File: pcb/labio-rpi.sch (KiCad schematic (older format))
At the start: 7 parts, among them P1 CONN_02X20

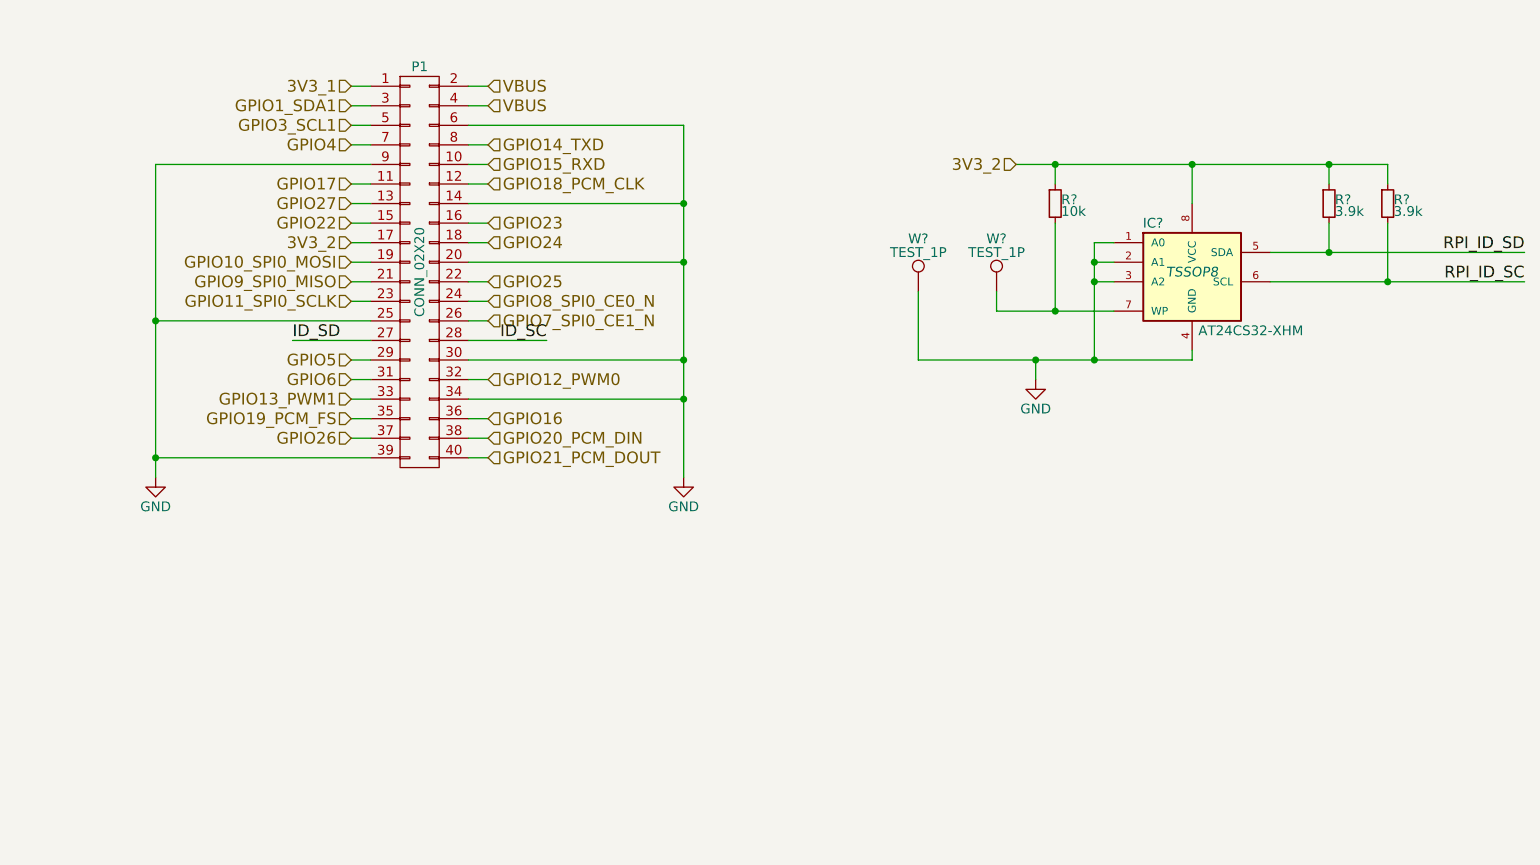
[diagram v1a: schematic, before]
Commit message: add imu sensors, make top level connections
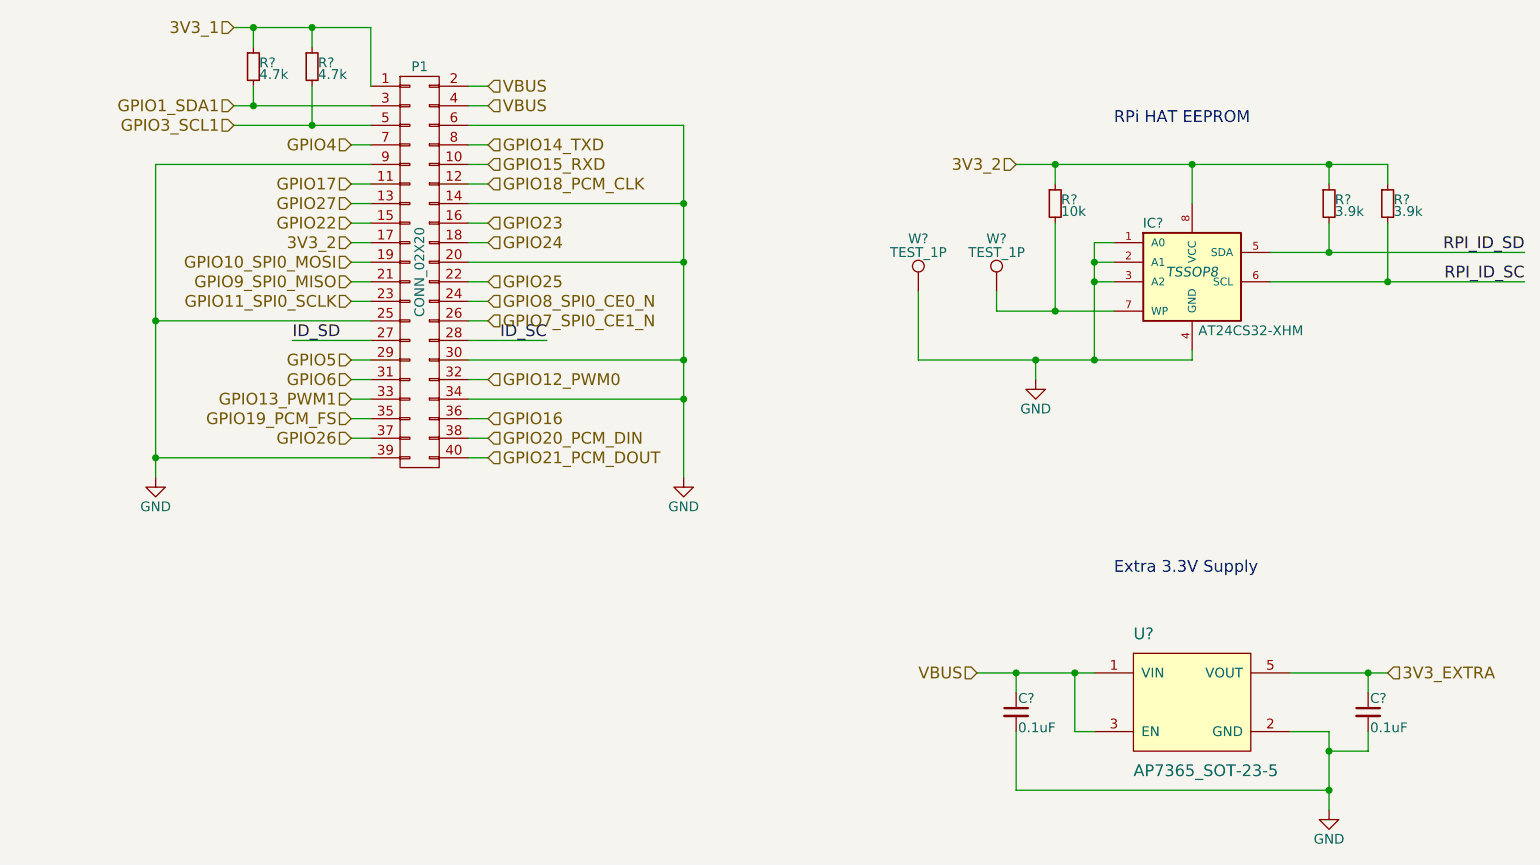
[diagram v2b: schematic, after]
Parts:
- added C? (x2): 0.1uF, symbol C_Small
- added R? (x2): 4.7k, symbol R_Small
- added U?: AP7365_SOT-23-5, symbol AP7365_SOT-23-5
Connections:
- net 3V3_1: now also R?.1, R?.1
- net GND: now also C?.2, C?.2, U?.2 (GND)
- net GPIO1_SDA1: now also R?.2
- net GPIO3_SCL1: now also R?.2
- net VBUS: now also C?.1, U?.1 (VIN), U?.3 (EN)
- new net 3V3_EXTRA: C?.1, U?.5 (VOUT)
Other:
- note added: "Extra 3.3V Supply"
- note added: "RPi HAT EEPROM"
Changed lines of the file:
@@
 $Descr A4 11693 8268
 encoding utf-8
-Sheet 2 8
+Sheet 2 7
 Title ""
 Date ""
@@
 	3900 1400 4000 1400
 Wire Wire Line
-	4000 1300 3900 1300
+	4000 1300 3300 1300
 Wire Wire Line
-	3900 1200 4000 1200
-Wire Wire Line
-	4000 1100 3900 1100
+	3300 1200 4000 1200
 Text Label 4900 2400 2    60   ~ 0
 ID_SC
-Text HLabel 3900 1100 0    60   Input ~ 0
+Text HLabel 3300 800  0    60   Input ~ 0
 3V3_1
-Text HLabel 3900 1200 0    60   Input ~ 0
+Text HLabel 3300 1200 0    60   Input ~ 0
 GPIO1_SDA1
-Text HLabel 3900 1300 0    60   Input ~ 0
+Text HLabel 3300 1300 0    60   Input ~ 0
 GPIO3_SCL1
 Text HLabel 3900 1400 0    60   Input ~ 0
@@
 	3600 2400 4000 2400
 Wire Wire Line
-	2900 1500 2900 2300
-Wire Wire Line
-	2900 2300 2900 3000
-Wire Wire Line
-	2900 3000 2900 3100
+	2900 1500 2900 3100
 Connection ~ 2900 3000
 Connection ~ 2900 2300
@@
 	4500 2400 4900 2400
 Wire Wire Line
-	5600 1300 5600 1700
-Wire Wire Line
-	5600 1700 5600 2000
-Wire Wire Line
-	5600 2000 5600 2500
-Wire Wire Line
-	5600 2500 5600 2700
-Wire Wire Line
-	5600 2700 5600 3100
+	5600 1300 5600 3100
 Connection ~ 5600 2700
 Connection ~ 5600 2500
@@
 	8200 2500 8200 2450
 Wire Wire Line
-	6800 2500 7400 2500
-Wire Wire Line
-	7400 2500 7700 2500
+	6800 2500 8200 2500
 Wire Wire Line
-	7700 2500 8200 2500
-Wire Wire Line
-	7200 2250 7500 2250
-Wire Wire Line
-	7500 2250 7800 2250
+	7200 2250 7800 2250
 Wire Wire Line
 	7500 2250 7500 1800
@@
 	7700 2100 7800 2100
 Wire Wire Line
-	7700 1900 7700 2000
-Wire Wire Line
-	7700 2000 7700 2100
-Wire Wire Line
-	7700 2100 7700 2500
+	7700 1900 7700 2500
 Connection ~ 7700 2500
 Wire Wire Line
@@
 Connection ~ 7700 2000
 Wire Wire Line
-	8600 1950 8900 1950
+	8600 1950 9900 1950
 Wire Wire Line
-	8900 1950 9900 1950
-Wire Wire Line
-	8600 2100 9200 2100
-Wire Wire Line
-	9200 2100 9900 2100
+	8600 2100 9900 2100
 Wire Wire Line
 	8900 1800 8900 1950
@@
 Connection ~ 9200 2100
 Wire Wire Line
-	7300 1500 7500 1500
-Wire Wire Line
-	7500 1500 8200 1500
-Wire Wire Line
-	8200 1500 8900 1500
-Wire Wire Line
-	8900 1500 9200 1500
+	7300 1500 9200 1500
 Wire Wire Line
 	7500 1500 7500 1600
@@
 Text HLabel 7300 1500 0    60   Input ~ 0
 3V3_2
+$Comp
+L R_Small R?
+U 1 1 5766CCA0
+P 3700 1000
+F 0 "R?" H 3730 1020 50  0000 L CNN
+F 1 "4.7k" H 3730 960 50  0000 L CNN
+F 2 "" H 3700 1000 50  0000 C CNN
+F 3 "" H 3700 1000 50  0000 C CNN
+	1    3700 1000
+	1    0    0    -1
+$EndComp
+$Comp
+L R_Small R?
+U 1 1 5766CD8E
+P 3400 1000
+F 0 "R?" H 3430 1020 50  0000 L CNN
+F 1 "4.7k" H 3430 960 50  0000 L CNN
+F 2 "" H 3400 1000 50  0000 C CNN
+F 3 "" H 3400 1000 50  0000 C CNN
+	1    3400 1000
+	1    0    0    -1
+$EndComp
+Wire Wire Line
+	4000 1100 4000 800
+Wire Wire Line
+	4000 800  3300 800
+Wire Wire Line
+	3400 900  3400 800
+Connection ~ 3400 800
+Wire Wire Line
+	3400 1100 3400 1200
+Connection ~ 3400 1200
+Wire Wire Line
+	3700 900  3700 800
+Connection ~ 3700 800
+Wire Wire Line
+	3700 1100 3700 1300
+Connection ~ 3700 1300
+$Comp
+L AP7365_SOT-23-5 U?
+U 1 1 5767CCA9
+P 8200 4250
+F 0 "U?" H 7900 4600 60  0000 L CNN
+F 1 "AP7365_SOT-23-5" H 7900 3900 60  0000 L CNN
+F 2 "" H 8200 4250 60  0000 C CNN
+F 3 "" H 8200 4250 60  0000 C CNN
+	1    8200 4250
+	1    0    0    -1
+$EndComp
+Text Notes 7800 1300 0    60   ~ 0
+RPi HAT EEPROM
+Text Notes 7800 3600 0    60   ~ 0
+Extra 3.3V Supply
+$Comp
+L C_Small C?
+U 1 1 5767CDD0
+P 7300 4300
+F 0 "C?" H 7310 4370 50  0000 L CNN
+F 1 "0.1uF" H 7310 4220 50  0000 L CNN
+F 2 "" H 7300 4300 50  0000 C CNN
+F 3 "" H 7300 4300 50  0000 C CNN
+	1    7300 4300
+	1    0    0    -1
+$EndComp
+$Comp
+L C_Small C?
+U 1 1 5767CE24
+P 9100 4300
+F 0 "C?" H 9110 4370 50  0000 L CNN
+F 1 "0.1uF" H 9110 4220 50  0000 L CNN
+F 2 "" H 9100 4300 50  0000 C CNN
+F 3 "" H 9100 4300 50  0000 C CNN
+	1    9100 4300
+	1    0    0    -1
+$EndComp
+$Comp
+L GND #PWR?
+U 1 1 5767CF14
+P 8900 4800
+F 0 "#PWR?" H 8900 4550 50  0001 C CNN
+F 1 "GND" H 8900 4650 50  0000 C CNN
+F 2 "" H 8900 4800 50  0000 C CNN
+F 3 "" H 8900 4800 50  0000 C CNN
+	1    8900 4800
+	1    0    0    -1
+$EndComp
+Text HLabel 7100 4100 0    60   Input ~ 0
+VBUS
+Wire Wire Line
+	7100 4100 7700 4100
+Wire Wire Line
+	7300 4200 7300 4100
+Connection ~ 7300 4100
+Wire Wire Line
+	7700 4400 7600 4400
+Wire Wire Line
+	7600 4400 7600 4100
+Connection ~ 7600 4100
+Wire Wire Line
+	7300 4400 7300 4700
+Wire Wire Line
+	7300 4700 8900 4700
+Wire Wire Line
+	8900 4400 8900 4800
+Wire Wire Line
+	8900 4400 8700 4400
+Connection ~ 8900 4700
+Wire Wire Line
+	9100 4400 9100 4500
+Wire Wire Line
+	9100 4500 8900 4500
+Connection ~ 8900 4500
+Wire Wire Line
+	8700 4100 9200 4100
+Wire Wire Line
+	9100 4200 9100 4100
+Connection ~ 9100 4100
+Text HLabel 9200 4100 2    60   Input ~ 0
+3V3_EXTRA
 $EndSCHEMATC

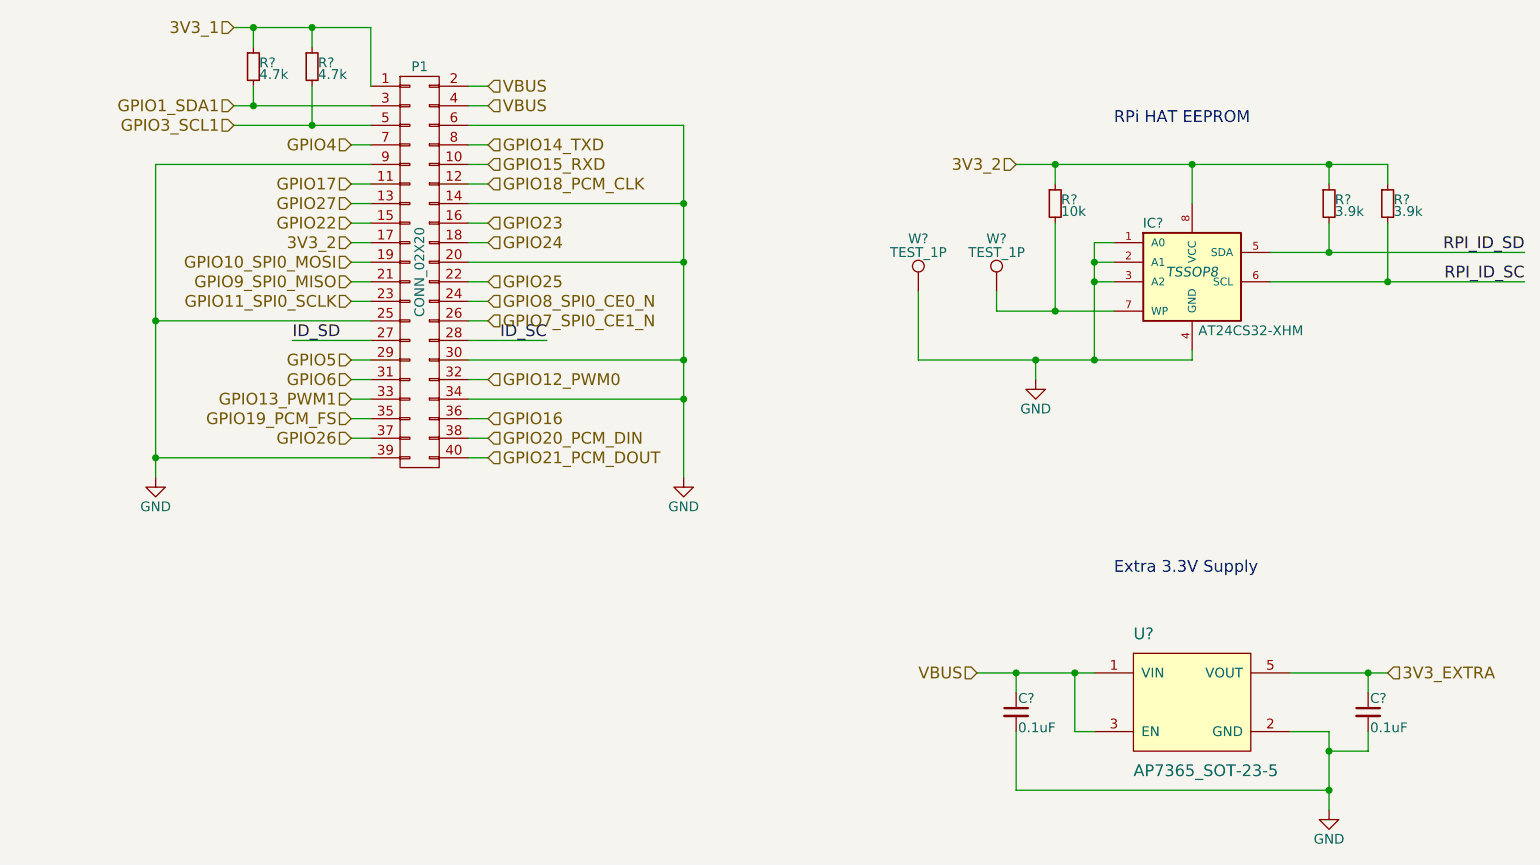
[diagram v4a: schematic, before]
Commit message: make extra footprints. start floorplan. fix display nets. add power expansion header.
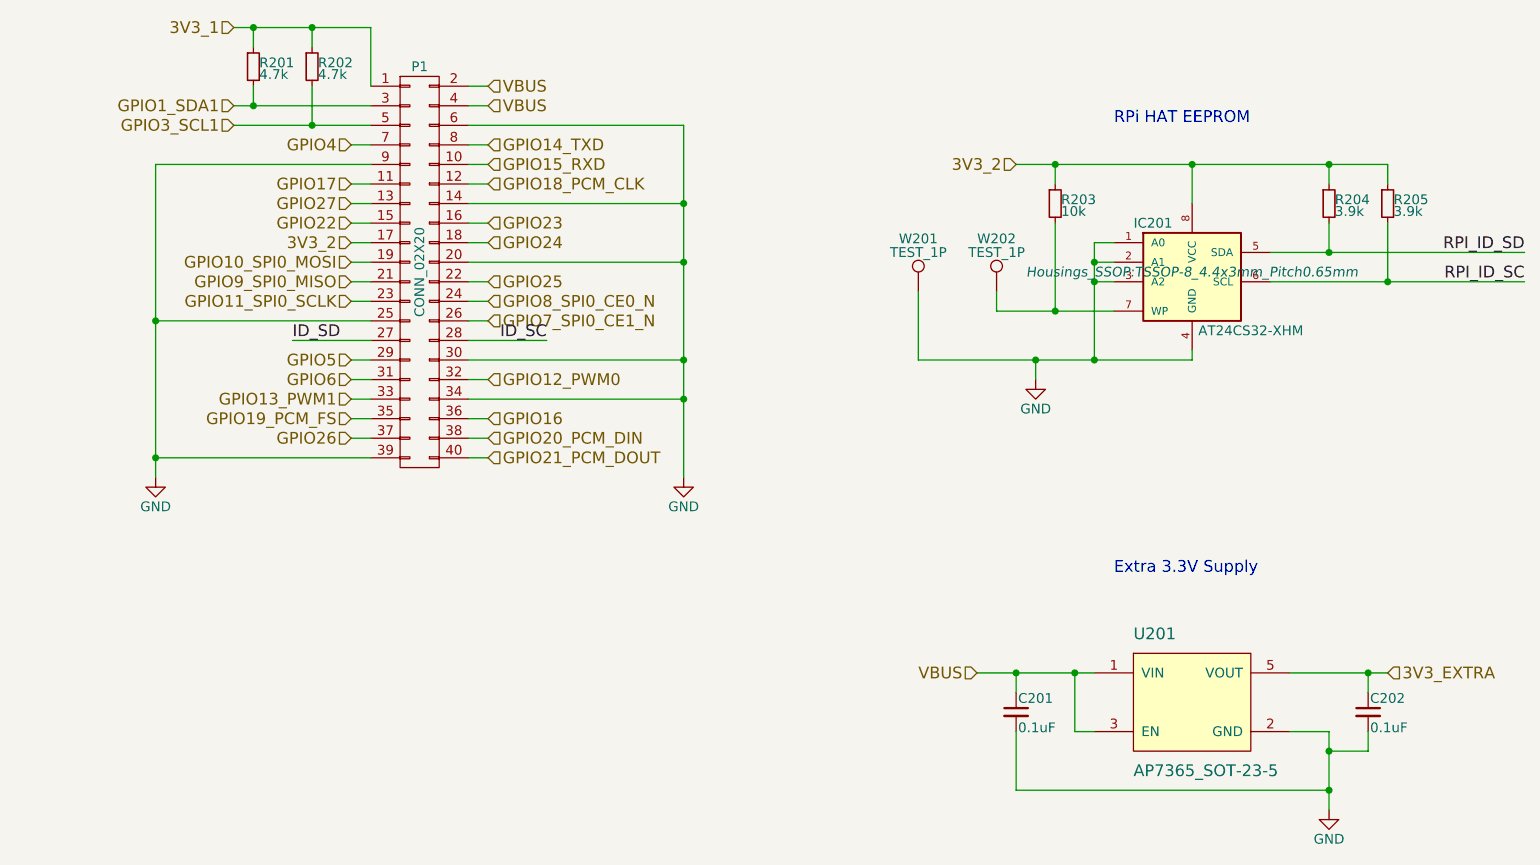
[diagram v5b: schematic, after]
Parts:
- C201, C202: renamed from C?; footprint (none) -> Capacitors_SMD:C_0603
- IC201: renamed from IC?; footprint TSSOP8 -> Housings_SSOP:TSSOP-8_4.4x3mm_Pitch0.65mm
- P1: footprint (none) -> labio-special:Pin_Header_Straight_TH-SMT_2x20
- R201, R202, R203, R204, R205: renamed from R?; footprint (none) -> Resistors_SMD:R_0603
- U201: renamed from U?; footprint (none) -> TO_SOT_Packages_SMD:SOT-23-5
- W201, W202: renamed from W?; footprint (none) -> Measurement_Points:Measurement_Point_Round-SMD-Pad_Small
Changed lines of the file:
@@
 $Descr A4 11693 8268
 encoding utf-8
-Sheet 2 8
+Sheet 2 9
 Title ""
 Date ""
@@
 F 0 "P1" H 4250 3100 50  0000 C CNN
 F 1 "CONN_02X20" V 4250 2050 50  0000 C CNN
-F 2 "" H 4250 1100 50  0000 C CNN
+F 2 "labio-special:Pin_Header_Straight_TH-SMT_2x20" H 4250 1100 50  0001 C CNN
 F 3 "" H 4250 1100 50  0000 C CNN
 	1    4250 2050
@@
 	3900 2900 4000 2900
 $Comp
-L GND #PWR?
+L GND #PWR01
 U 1 1 57477DAC
 P 2900 3100
-F 0 "#PWR?" H 2900 2850 50  0001 C CNN
+F 0 "#PWR01" H 2900 2850 50  0001 C CNN
 F 1 "GND" H 2900 2950 50  0000 C CNN
 F 2 "" H 2900 3100 50  0000 C CNN
@@
 GPIO21_PCM_DOUT
 $Comp
-L GND #PWR?
+L GND #PWR02
 U 1 1 5747813A
 P 5600 3100
-F 0 "#PWR?" H 5600 2850 50  0001 C CNN
+F 0 "#PWR02" H 5600 2850 50  0001 C CNN
 F 1 "GND" H 5600 2950 50  0000 C CNN
 F 2 "" H 5600 3100 50  0000 C CNN
@@
 Connection ~ 5600 1700
 $Comp
-L AT24CS32-XHM IC?
+L AT24CS32-XHM IC201
 U 1 1 57478830
 P 8200 2050
-F 0 "IC?" H 8000 2300 50  0000 C CNN
+F 0 "IC201" H 8000 2300 50  0000 C CNN
 F 1 "AT24CS32-XHM" H 8500 1750 50  0000 C CNN
-F 2 "TSSOP8" H 8200 2050 50  0000 C CIN
+F 2 "Housings_SSOP:TSSOP-8_4.4x3mm_Pitch0.65mm" H 8200 2050 50  0000 C CIN
 F 3 "" H 8200 2050 50  0000 C CNN
 	1    8200 2050
@@
 $EndComp
 $Comp
-L R_Small R?
+L R_Small R203
 U 1 1 57478872
 P 7500 1700
-F 0 "R?" H 7530 1720 50  0000 L CNN
+F 0 "R203" H 7530 1720 50  0000 L CNN
 F 1 "10k" H 7530 1660 50  0000 L CNN
-F 2 "" H 7500 1700 50  0000 C CNN
+F 2 "Resistors_SMD:R_0603" H 7500 1700 50  0001 C CNN
 F 3 "" H 7500 1700 50  0000 C CNN
 	1    7500 1700
@@
 $EndComp
 $Comp
-L R_Small R?
+L R_Small R204
 U 1 1 574788B2
 P 8900 1700
-F 0 "R?" H 8930 1720 50  0000 L CNN
+F 0 "R204" H 8930 1720 50  0000 L CNN
 F 1 "3.9k" H 8930 1660 50  0000 L CNN
-F 2 "" H 8900 1700 50  0000 C CNN
+F 2 "Resistors_SMD:R_0603" H 8900 1700 50  0001 C CNN
 F 3 "" H 8900 1700 50  0000 C CNN
 	1    8900 1700
@@
 $EndComp
 $Comp
-L R_Small R?
+L R_Small R205
 U 1 1 574788E9
 P 9200 1700
-F 0 "R?" H 9230 1720 50  0000 L CNN
+F 0 "R205" H 9230 1720 50  0000 L CNN
 F 1 "3.9k" H 9230 1660 50  0000 L CNN
-F 2 "" H 9200 1700 50  0000 C CNN
+F 2 "Resistors_SMD:R_0603" H 9200 1700 50  0001 C CNN
 F 3 "" H 9200 1700 50  0000 C CNN
 	1    9200 1700
@@
 $EndComp
 $Comp
-L GND #PWR?
+L GND #PWR03
 U 1 1 574789A2
 P 7400 2600
-F 0 "#PWR?" H 7400 2350 50  0001 C CNN
+F 0 "#PWR03" H 7400 2350 50  0001 C CNN
 F 1 "GND" H 7400 2450 50  0000 C CNN
 F 2 "" H 7400 2600 50  0000 C CNN
@@
 Connection ~ 8900 1500
 $Comp
-L TEST_1P W?
+L TEST_1P W202
 U 1 1 57478E02
 P 7200 2150
-F 0 "W?" H 7200 2420 50  0000 C CNN
+F 0 "W202" H 7200 2420 50  0000 C CNN
 F 1 "TEST_1P" H 7200 2350 50  0000 C CNN
-F 2 "" H 7400 2150 50  0000 C CNN
+F 2 "Measurement_Points:Measurement_Point_Round-SMD-Pad_Small" H 7400 2150 50  0001 C CNN
 F 3 "" H 7400 2150 50  0000 C CNN
 	1    7200 2150
@@
 $EndComp
 $Comp
-L TEST_1P W?
+L TEST_1P W201
 U 1 1 57478E49
 P 6800 2150
-F 0 "W?" H 6800 2420 50  0000 C CNN
+F 0 "W201" H 6800 2420 50  0000 C CNN
 F 1 "TEST_1P" H 6800 2350 50  0000 C CNN
-F 2 "" H 7000 2150 50  0000 C CNN
+F 2 "Measurement_Points:Measurement_Point_Round-SMD-Pad_Small" H 7000 2150 50  0001 C CNN
 F 3 "" H 7000 2150 50  0000 C CNN
 	1    6800 2150
@@
 3V3_2
 $Comp
-L R_Small R?
+L R_Small R202
 U 1 1 5766CCA0
 P 3700 1000
-F 0 "R?" H 3730 1020 50  0000 L CNN
+F 0 "R202" H 3730 1020 50  0000 L CNN
 F 1 "4.7k" H 3730 960 50  0000 L CNN
-F 2 "" H 3700 1000 50  0000 C CNN
+F 2 "Resistors_SMD:R_0603" H 3700 1000 50  0001 C CNN
 F 3 "" H 3700 1000 50  0000 C CNN
 	1    3700 1000
@@
 $EndComp
 $Comp
-L R_Small R?
+L R_Small R201
 U 1 1 5766CD8E
 P 3400 1000
-F 0 "R?" H 3430 1020 50  0000 L CNN
+F 0 "R201" H 3430 1020 50  0000 L CNN
 F 1 "4.7k" H 3430 960 50  0000 L CNN
-F 2 "" H 3400 1000 50  0000 C CNN
+F 2 "Resistors_SMD:R_0603" H 3400 1000 50  0001 C CNN
 F 3 "" H 3400 1000 50  0000 C CNN
 	1    3400 1000
@@
 Connection ~ 3700 1300
 $Comp
-L AP7365_SOT-23-5 U?
+L AP7365_SOT-23-5 U201
 U 1 1 5767CCA9
 P 8200 4250
-F 0 "U?" H 7900 4600 60  0000 L CNN
+F 0 "U201" H 7900 4600 60  0000 L CNN
 F 1 "AP7365_SOT-23-5" H 7900 3900 60  0000 L CNN
-F 2 "" H 8200 4250 60  0000 C CNN
+F 2 "TO_SOT_Packages_SMD:SOT-23-5" H 8200 4250 60  0001 C CNN
 F 3 "" H 8200 4250 60  0000 C CNN
 	1    8200 4250
@@
 Extra 3.3V Supply
 $Comp
-L C_Small C?
+L C_Small C201
 U 1 1 5767CDD0
 P 7300 4300
-F 0 "C?" H 7310 4370 50  0000 L CNN
+F 0 "C201" H 7310 4370 50  0000 L CNN
 F 1 "0.1uF" H 7310 4220 50  0000 L CNN
-F 2 "" H 7300 4300 50  0000 C CNN
+F 2 "Capacitors_SMD:C_0603" H 7300 4300 50  0001 C CNN
 F 3 "" H 7300 4300 50  0000 C CNN
 	1    7300 4300
@@
 $EndComp
 $Comp
-L C_Small C?
+L C_Small C202
 U 1 1 5767CE24
 P 9100 4300
-F 0 "C?" H 9110 4370 50  0000 L CNN
+F 0 "C202" H 9110 4370 50  0000 L CNN
 F 1 "0.1uF" H 9110 4220 50  0000 L CNN
-F 2 "" H 9100 4300 50  0000 C CNN
+F 2 "Capacitors_SMD:C_0603" H 9100 4300 50  0001 C CNN
 F 3 "" H 9100 4300 50  0000 C CNN
 	1    9100 4300
@@
 $EndComp
 $Comp
-L GND #PWR?
+L GND #PWR04
 U 1 1 5767CF14
 P 8900 4800
-F 0 "#PWR?" H 8900 4550 50  0001 C CNN
+F 0 "#PWR04" H 8900 4550 50  0001 C CNN
 F 1 "GND" H 8900 4650 50  0000 C CNN
 F 2 "" H 8900 4800 50  0000 C CNN
